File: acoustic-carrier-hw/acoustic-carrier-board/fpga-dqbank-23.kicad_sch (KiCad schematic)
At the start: 13 parts, among them IC1 ECP5-BGA256

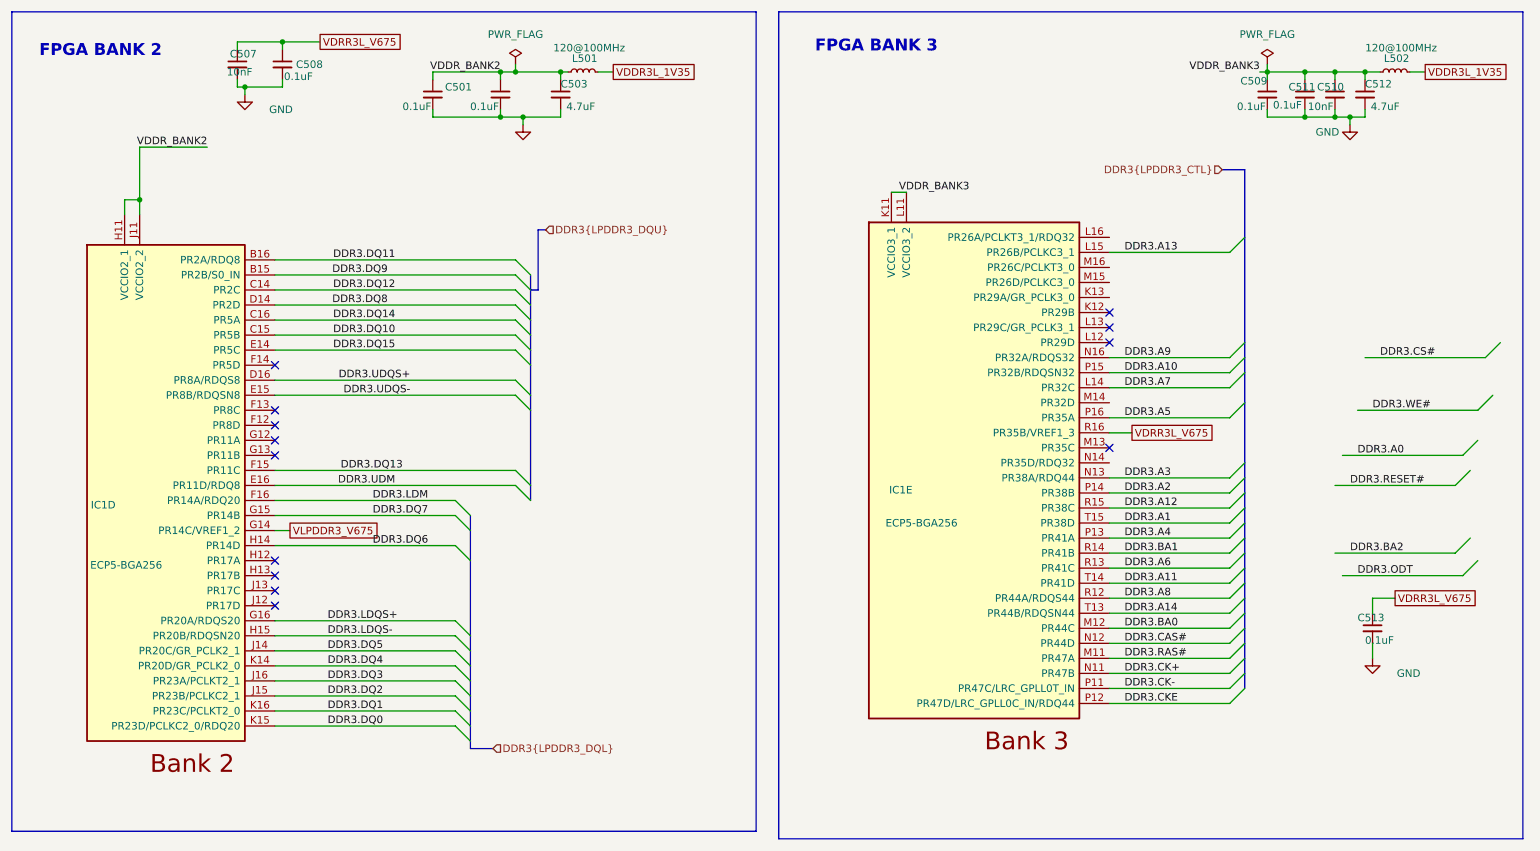
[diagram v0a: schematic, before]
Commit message: [carrier] Routed LDQ group and CMD-CTRL bus
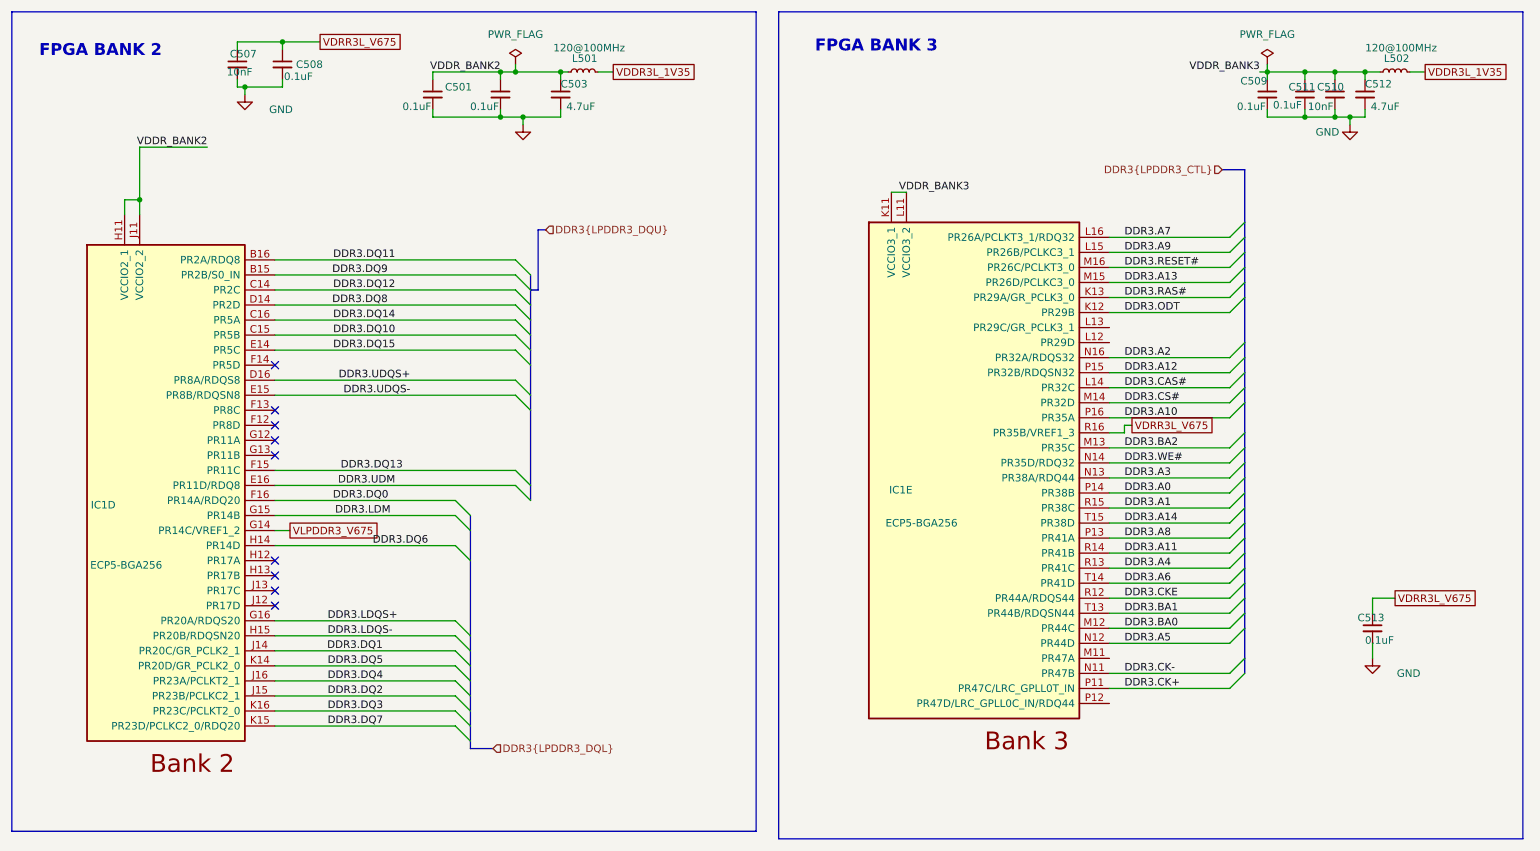
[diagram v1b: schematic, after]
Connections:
- net DDR3.A0: now also IC1.P14 (PR38B)
- net DDR3.A1: now also IC1.R15 (PR38C); no longer IC1.T15 (PR38D)
- net DDR3.A10: now also IC1.P16 (PR35A); no longer IC1.P15 (PR32B/RDQSN32)
- net DDR3.A11: now also IC1.R14 (PR41B); no longer IC1.T14 (PR41D)
- net DDR3.A12: now also IC1.P15 (PR32B/RDQSN32); no longer IC1.R15 (PR38C)
- net DDR3.A13: now also IC1.M15 (PR26D/PCLKC3_0); no longer IC1.L15 (PR26B/PCLKC3_1)
- net DDR3.A14: now also IC1.T15 (PR38D); no longer IC1.T13 (PR44B/RDQSN44)
- net DDR3.A2: now also IC1.N16 (PR32A/RDQS32); no longer IC1.P14 (PR38B)
- net DDR3.A4: now also IC1.R13 (PR41C); no longer IC1.P13 (PR41A)
- net DDR3.A5: now also IC1.N12 (PR44D); no longer IC1.P16 (PR35A)
- net DDR3.A6: now also IC1.T14 (PR41D); no longer IC1.R13 (PR41C)
- net DDR3.A7: now also IC1.L16 (PR26A/PCLKT3_1/RDQ32); no longer IC1.L14 (PR32C)
- net DDR3.A8: now also IC1.P13 (PR41A); no longer IC1.R12 (PR44A/RDQS44)
- net DDR3.A9: now also IC1.L15 (PR26B/PCLKC3_1); no longer IC1.N16 (PR32A/RDQS32)
- net DDR3.BA1: now also IC1.T13 (PR44B/RDQSN44); no longer IC1.R14 (PR41B)
- net DDR3.BA2: now also IC1.M13 (PR35C)
- net DDR3.CAS#: now also IC1.L14 (PR32C); no longer IC1.N12 (PR44D)
- net DDR3.CK+: now also IC1.P11 (PR47C/LRC_GPLL0T_IN); no longer IC1.N11 (PR47B)
- net DDR3.CK-: now also IC1.N11 (PR47B); no longer IC1.P11 (PR47C/LRC_GPLL0T_IN)
- net DDR3.CKE: now also IC1.R12 (PR44A/RDQS44); no longer IC1.P12 (PR47D/LRC_GPLL0C_IN/RDQ44)
- net DDR3.CS#: now also IC1.M14 (PR32D)
- net DDR3.DQ0: now also IC1.F16 (PR14A/RDQ20); no longer IC1.K15 (PR23D/PCLKC2_0/RDQ20)
- net DDR3.DQ1: now also IC1.J14 (PR20C/GR_PCLK2_1); no longer IC1.K16 (PR23C/PCLKT2_0)
- net DDR3.DQ3: now also IC1.K16 (PR23C/PCLKT2_0); no longer IC1.J16 (PR23A/PCLKT2_1)
- net DDR3.DQ4: now also IC1.J16 (PR23A/PCLKT2_1); no longer IC1.K14 (PR20D/GR_PCLK2_0)
- net DDR3.DQ5: now also IC1.K14 (PR20D/GR_PCLK2_0); no longer IC1.J14 (PR20C/GR_PCLK2_1)
- net DDR3.DQ7: now also IC1.K15 (PR23D/PCLKC2_0/RDQ20); no longer IC1.G15 (PR14B)
- net DDR3.LDM: now also IC1.G15 (PR14B); no longer IC1.F16 (PR14A/RDQ20)
- net DDR3.ODT: now also IC1.K12 (PR29B)
- net DDR3.RAS#: now also IC1.K13 (PR29A/GR_PCLK3_0); no longer IC1.M11 (PR47A)
- net DDR3.RESET#: now also IC1.M16 (PR26C/PCLKT3_0)
- net DDR3.WE#: now also IC1.N14 (PR35D/RDQ32)
- no-connect marks 13 -> 9

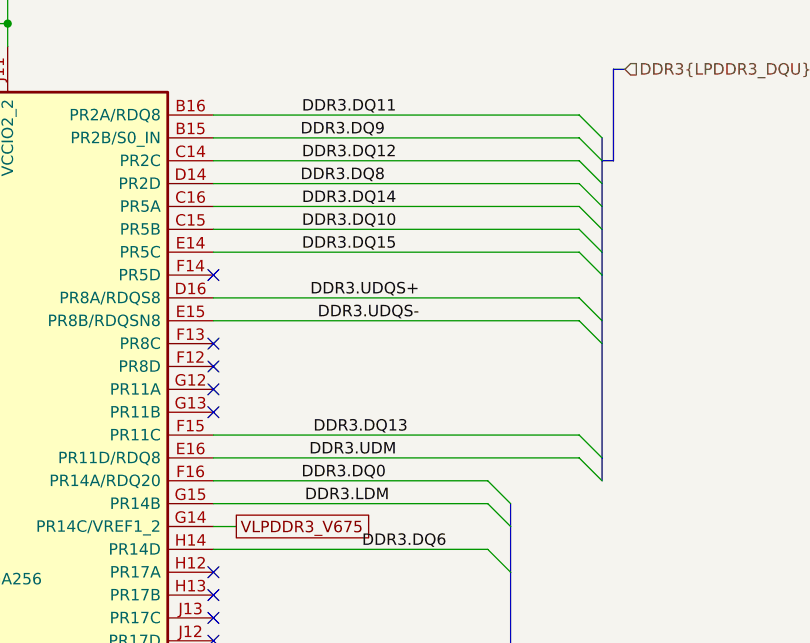
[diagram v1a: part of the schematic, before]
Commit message: [carrier] Connected part of DQU
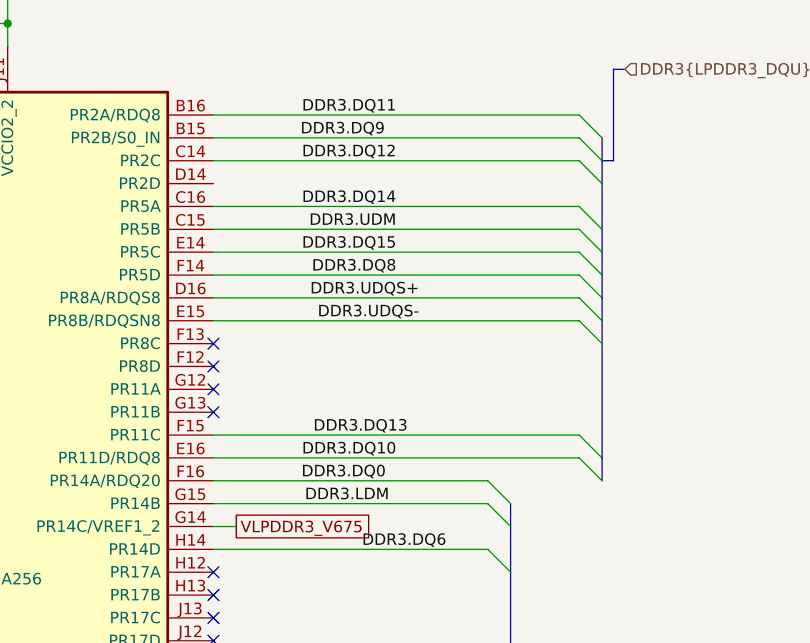
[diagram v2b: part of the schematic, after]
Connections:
- net DDR3.DQ10: now also IC1.E16 (PR11D/RDQ8); no longer IC1.C15 (PR5B)
- net DDR3.DQ8: now also IC1.F14 (PR5D); no longer IC1.D14 (PR2D)
- net DDR3.UDM: now also IC1.C15 (PR5B); no longer IC1.E16 (PR11D/RDQ8)
- no-connect marks 9 -> 8

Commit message: [carrier] Routed LPDDR3 without length matching
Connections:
- net DDR3.DQ11: now also IC1.E14 (PR5C); no longer IC1.B16 (PR2A/RDQ8)
- net DDR3.DQ12: now also IC1.B16 (PR2A/RDQ8); no longer IC1.C14 (PR2C)
- net DDR3.DQ13: now also IC1.C16 (PR5A); no longer IC1.F15 (PR11C)
- net DDR3.DQ14: now also IC1.C14 (PR2C); no longer IC1.C16 (PR5A)
- net DDR3.DQ15: now also IC1.C15 (PR5B); no longer IC1.E14 (PR5C)
- net DDR3.DQ9: now also IC1.D14 (PR2D); no longer IC1.B15 (PR2B/S0_IN)
- net DDR3.UDM: now also IC1.F13 (PR8C); no longer IC1.C15 (PR5B)
- no-connect marks 8 -> 13

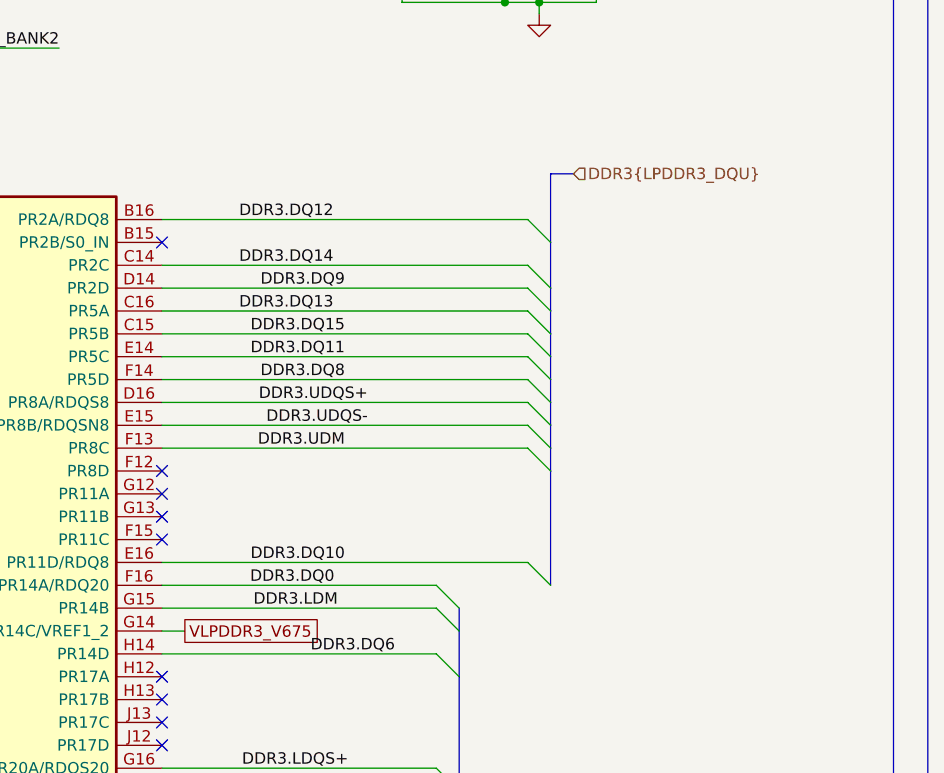
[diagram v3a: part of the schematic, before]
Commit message: [carrier] Routing out RGMII interface
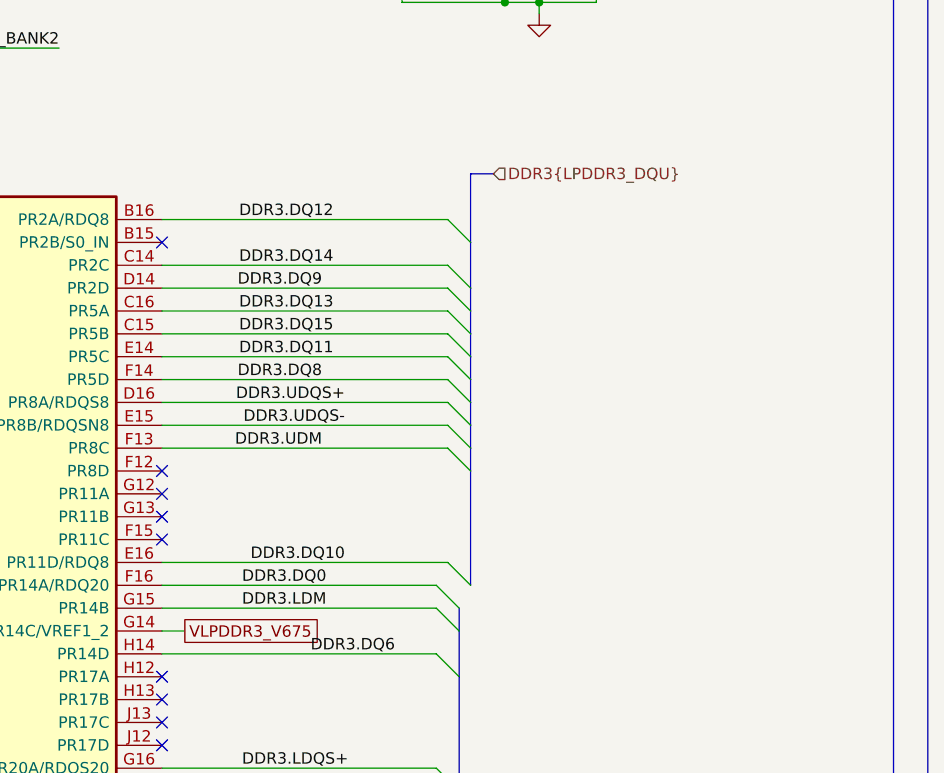
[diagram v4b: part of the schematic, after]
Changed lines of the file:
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@@
 	)
 	(bus_entry
-		(at 114.3 90.17)
+		(at 105.41 90.17)
 		(size -2.54 -2.54)
 		(stroke
@@
 	)
 	(bus_entry
-		(at 111.76 72.39)
+		(at 102.87 72.39)
 		(size 2.54 2.54)
 		(stroke
@@
 	)
 	(bus_entry
-		(at 114.3 64.77)
+		(at 105.41 64.77)
 		(size -2.54 -2.54)
 		(stroke
@@
 	)
 	(bus_entry
-		(at 114.3 85.09)
+		(at 105.41 85.09)
 		(size -2.54 -2.54)
 		(stroke
@@
 	)
 	(bus_entry
-		(at 114.3 80.01)
+		(at 105.41 80.01)
 		(size -2.54 -2.54)
 		(stroke
@@
 	)
 	(bus_entry
-		(at 114.3 87.63)
+		(at 105.41 87.63)
 		(size -2.54 -2.54)
 		(stroke
@@
 	)
 	(bus_entry
-		(at 114.3 72.39)
+		(at 105.41 72.39)
 		(size -2.54 -2.54)
 		(stroke
@@
 	)
 	(bus_entry
-		(at 114.3 82.55)
+		(at 105.41 82.55)
 		(size -2.54 -2.54)
 		(stroke
@@
 	)
 	(bus_entry
-		(at 114.3 69.85)
+		(at 105.41 69.85)
 		(size -2.54 -2.54)
 		(stroke
@@
 	)
 	(bus_entry
-		(at 111.76 100.33)
+		(at 102.87 100.33)
 		(size 2.54 2.54)
 		(stroke
@@
 	)
 	(bus_entry
-		(at 114.3 77.47)
+		(at 105.41 77.47)
 		(size -2.54 -2.54)
 		(stroke
@@
 	(bus
 		(pts
-			(xy 114.3 85.09) (xy 114.3 82.55)
-		)
-		(stroke
-			(width 0)
-			(type default)
-		)
-	)
-	(wire
-		(pts
-			(xy 71.12 69.85) (xy 111.76 69.85)
+			(xy 105.41 85.09) (xy 105.41 82.55)
+		)
+		(stroke
+			(width 0)
+			(type default)
+		)
+	)
+	(wire
+		(pts
+			(xy 71.12 69.85) (xy 102.87 69.85)
 		)
 		(stroke
@@
 	(bus
 		(pts
-			(xy 114.3 57.15) (xy 116.84 57.15)
+			(xy 105.41 57.15) (xy 107.95 57.15)
 		)
 		(stroke
@@
 	(bus
 		(pts
-			(xy 114.3 64.77) (xy 114.3 69.85)
+			(xy 105.41 64.77) (xy 105.41 69.85)
 		)
 		(stroke
@@
 	(bus
 		(pts
-			(xy 114.3 77.47) (xy 114.3 74.93)
+			(xy 105.41 77.47) (xy 105.41 74.93)
 		)
 		(stroke
@@
 	(wire
 		(pts
-			(xy 71.12 77.47) (xy 111.76 77.47)
+			(xy 71.12 77.47) (xy 102.87 77.47)
 		)
 		(stroke
@@
 	(wire
 		(pts
-			(xy 71.12 87.63) (xy 111.76 87.63)
+			(xy 71.12 87.63) (xy 102.87 87.63)
 		)
 		(stroke
@@
 	(bus
 		(pts
-			(xy 114.3 69.85) (xy 114.3 72.39)
+			(xy 105.41 69.85) (xy 105.41 72.39)
 		)
 		(stroke
@@
 	(wire
 		(pts
-			(xy 71.12 72.39) (xy 111.76 72.39)
+			(xy 71.12 72.39) (xy 102.87 72.39)
 		)
 		(stroke
@@
 	(wire
 		(pts
-			(xy 71.12 85.09) (xy 111.76 85.09)
+			(xy 71.12 85.09) (xy 102.87 85.09)
 		)
 		(stroke
@@
 	(bus
 		(pts
-			(xy 114.3 80.01) (xy 114.3 77.47)
+			(xy 105.41 80.01) (xy 105.41 77.47)
 		)
 		(stroke
@@
 	(wire
 		(pts
-			(xy 71.12 62.23) (xy 111.76 62.23)
+			(xy 71.12 62.23) (xy 102.87 62.23)
 		)
 		(stroke
@@
 	(bus
 		(pts
-			(xy 114.3 90.17) (xy 114.3 102.87)
+			(xy 105.41 90.17) (xy 105.41 102.87)
 		)
 		(stroke
@@
 	(wire
 		(pts
-			(xy 71.12 80.01) (xy 111.76 80.01)
+			(xy 71.12 80.01) (xy 102.87 80.01)
 		)
 		(stroke
@@
 	(wire
 		(pts
-			(xy 71.12 82.55) (xy 111.76 82.55)
+			(xy 71.12 82.55) (xy 102.87 82.55)
 		)
 		(stroke
@@
 	(wire
 		(pts
-			(xy 71.12 100.33) (xy 111.76 100.33)
+			(xy 71.12 100.33) (xy 102.87 100.33)
 		)
 		(stroke
@@
 	(bus
 		(pts
-			(xy 114.3 72.39) (xy 114.3 74.93)
+			(xy 105.41 72.39) (xy 105.41 74.93)
 		)
 		(stroke
@@
 	(wire
 		(pts
-			(xy 71.12 74.93) (xy 111.76 74.93)
-		)
-		(stroke
-			(width 0)
-			(type default)
-		)
-	)
-	(bus
-		(pts
-			(xy 114.3 64.77) (xy 114.3 57.15)
+			(xy 71.12 74.93) (xy 102.87 74.93)
+		)
+		(stroke
+			(width 0)
+			(type default)
+		)
+	)
+	(bus
+		(pts
+			(xy 105.41 64.77) (xy 105.41 57.15)
 		)
 		(stroke
@@
 	(bus
 		(pts
-			(xy 114.3 82.55) (xy 114.3 80.01)
+			(xy 105.41 82.55) (xy 105.41 80.01)
 		)
 		(stroke
@@
 	(wire
 		(pts
-			(xy 71.12 67.31) (xy 111.76 67.31)
+			(xy 71.12 67.31) (xy 102.87 67.31)
 		)
 		(stroke
@@
 	(bus
 		(pts
-			(xy 114.3 87.63) (xy 114.3 85.09)
+			(xy 105.41 87.63) (xy 105.41 85.09)
 		)
 		(stroke
@@
 	(bus
 		(pts
-			(xy 114.3 90.17) (xy 114.3 87.63)
+			(xy 105.41 90.17) (xy 105.41 87.63)
 		)
 		(stroke
@@
 	)
 	(label "DDR3.DQ11"
-		(at 91.44 77.47 180)
+		(at 90.17 77.47 180)
 		(effects
 			(font
@@
 	)
 	(label "DDR3.DQ0"
-		(at 80.9035 102.87 0)
+		(at 80.01 102.87 0)
 		(effects
 			(font
@@
 	)
 	(label "DDR3.DQ15"
-		(at 91.44 74.93 180)
+		(at 90.17 74.93 180)
 		(effects
 			(font
@@
 	)
 	(label "DDR3.DQ9"
-		(at 91.44 69.85 180)
+		(at 88.9 69.85 180)
 		(effects
 			(font
@@
 	)
 	(label "DDR3.DQ8"
-		(at 91.44 80.01 180)
+		(at 88.9 80.01 180)
 		(effects
 			(font
@@
 	)
 	(label "DDR3.LDM"
-		(at 81.28 105.41 0)
+		(at 80.01 105.41 0)
 		(effects
 			(font
@@
 	)
 	(label "DDR3.UDQS+"
-		(at 93.98 82.55 180)
+		(at 91.44 82.55 180)
 		(effects
 			(font
@@
 	)
 	(label "DDR3.UDM"
-		(at 91.44 87.63 180)
+		(at 88.9 87.63 180)
 		(effects
 			(font
@@
 	)
 	(label "DDR3.UDQS-"
-		(at 93.98 85.09 180)
+		(at 91.44 85.09 180)
 		(effects
 			(font
@@
 	(hierarchical_label "DDR3{LPDDR3_DQU}"
 		(shape input)
-		(at 116.84 57.15 0)
-		(effects
-			(font
+		(at 107.95 57.15 0)
+		(effects
+			(font
